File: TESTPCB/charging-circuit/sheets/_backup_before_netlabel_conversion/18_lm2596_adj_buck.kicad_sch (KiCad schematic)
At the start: 13 parts, among them J3 Conn_01x01_Pin, J4 Conn_01x01_Pin, J5 Conn_01x01_Pin, J6 Conn_01x01_Pin, U18 LM2596SX-5.0/NOPB

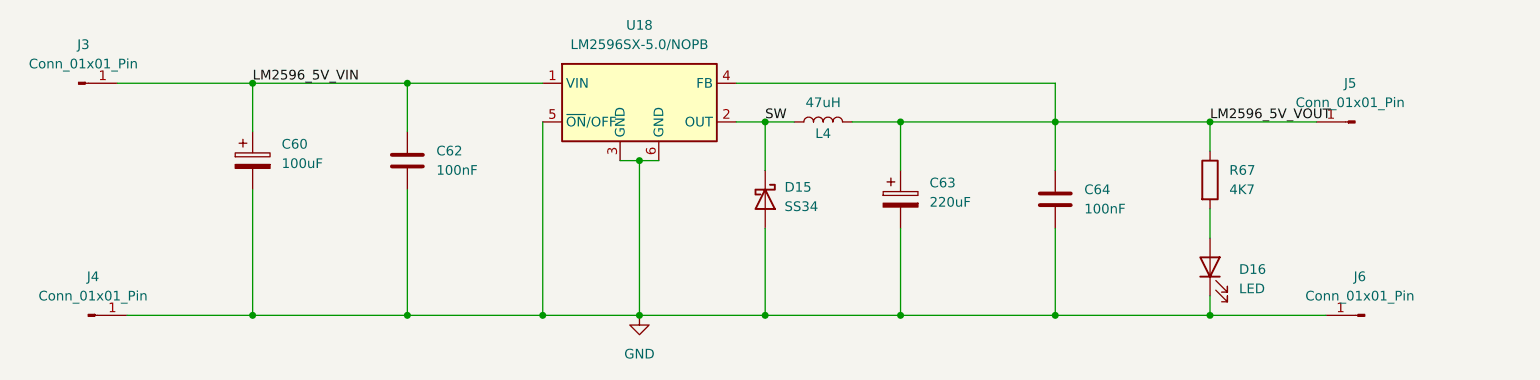
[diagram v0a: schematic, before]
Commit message: Fixed formatting issues, now the hierachal sheets are all labeled as net labels and when we want to expose their pins we will make them into hierchal or global pins
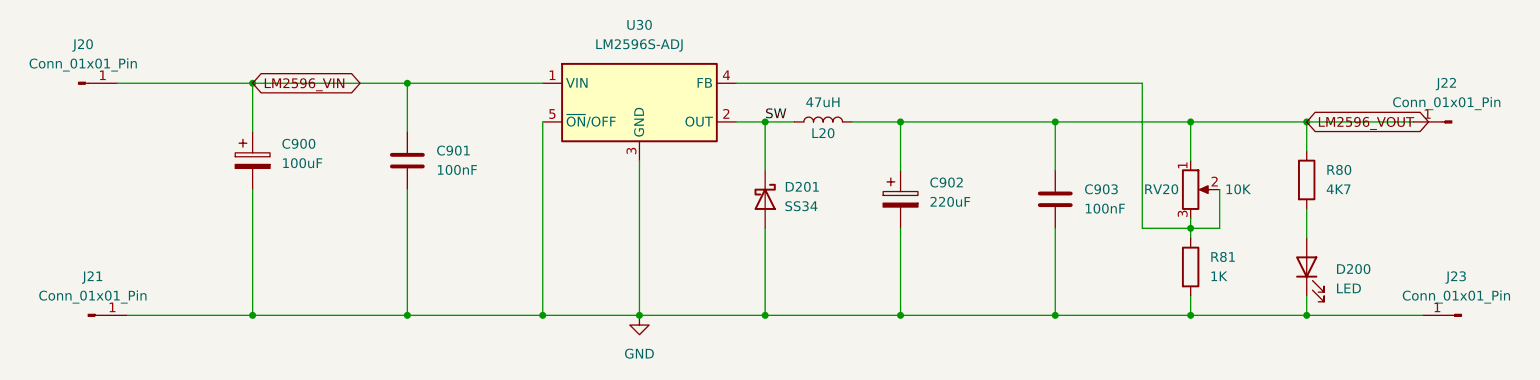
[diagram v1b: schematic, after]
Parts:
- removed U18: LM2596SX-5.0/NOPB, easyeda2kicad:TO-263-5_L10.2-W8.9-P1.70-TL, symbol easyeda2kicad:LM2596SX-5.0_NOPB
- added R81: 1K, Resistor_SMD:R_0603_1608Metric, symbol Device:R
- added RV20: 10K, Potentiometer_THT:Potentiometer_Bourns_3296W_Vertical, symbol Device:R_Potentiometer
- added U30: LM2596S-ADJ, Package_TO_SOT_SMD:TO-263-5_TabPin3, symbol Regulator_Switching:LM2596S-ADJ
- renumbered C60 to C900, C62 to C901, C63 to C902, C64 to C903, D16 to D200, D15 to D201, J3 to J20, J4 to J21, J5 to J22, J6 to J23, L4 to L20, R67 to R80
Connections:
- net GND: now also R81.2, U30.3 (GND), U30.5 (~{ON}/OFF)
- net SW: now also U30.2 (OUT)
- net LM2596_5V_VIN renamed LM2596_VIN
- net LM2596_VIN: now also U30.1 (VIN)
- net LM2596_5V_VOUT renamed LM2596_VOUT
- net LM2596_VOUT: now also RV20.1
- new net: R81.1, RV20.2, RV20.3, U30.4 (FB)
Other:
- moved on the sheet: D200, J22, J23, R80
